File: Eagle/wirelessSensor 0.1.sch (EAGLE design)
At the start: 26 parts, among them U1 HDC1080, U2 PIC16F1823-X_SL, X1 22-23-2021

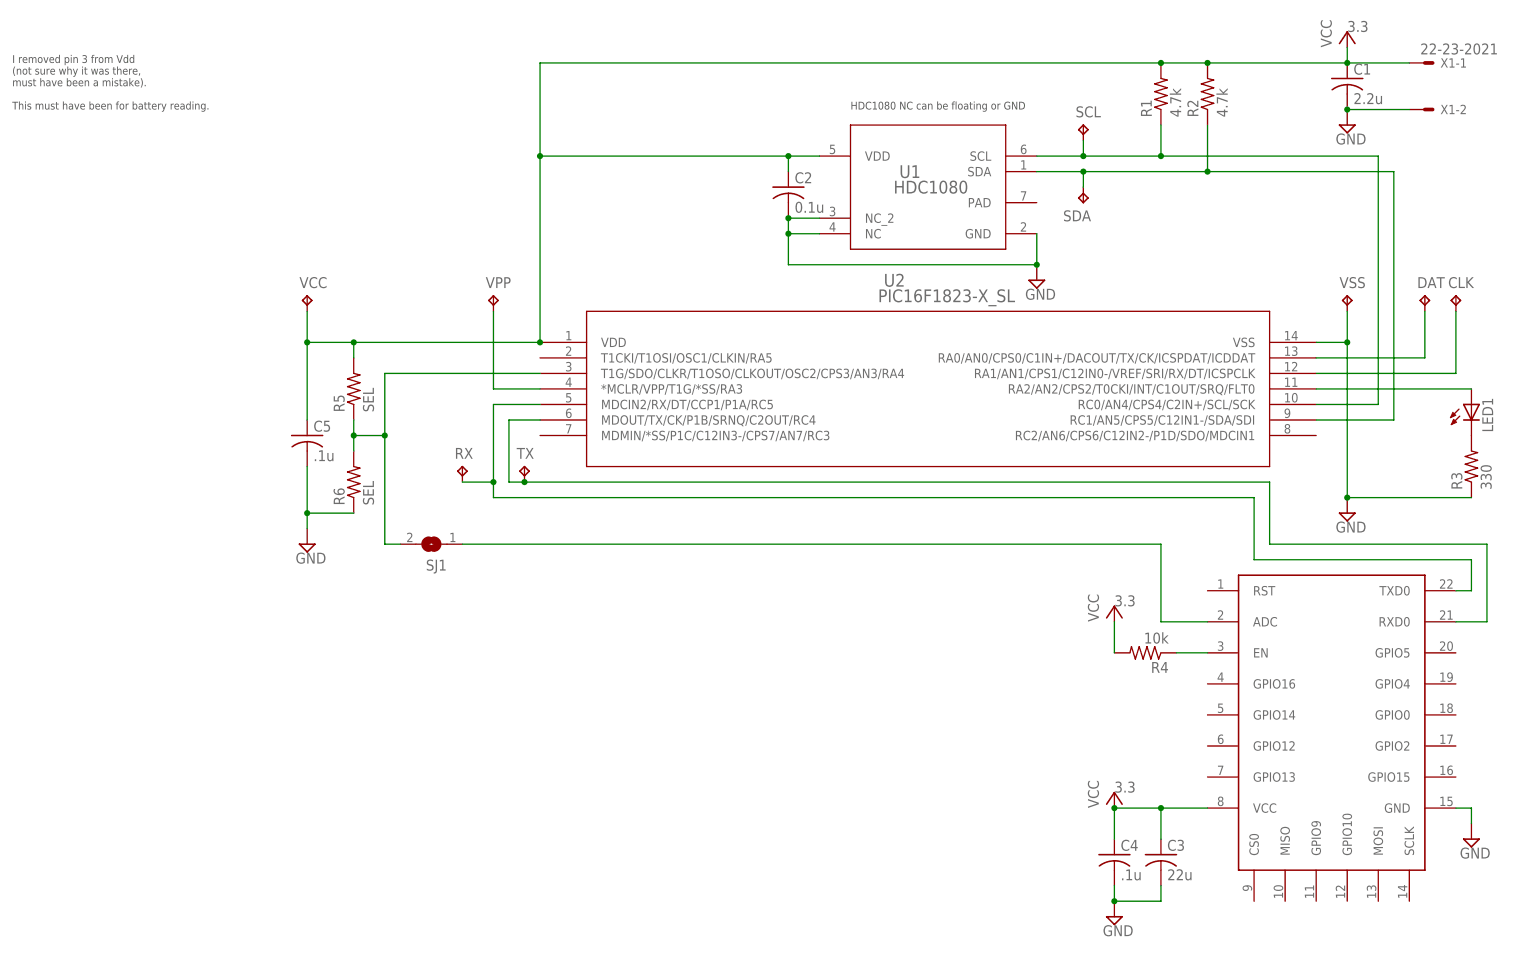
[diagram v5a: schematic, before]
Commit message: More work on the PCB, added some SeeedStudio specific files (cam generator, DRC rules)
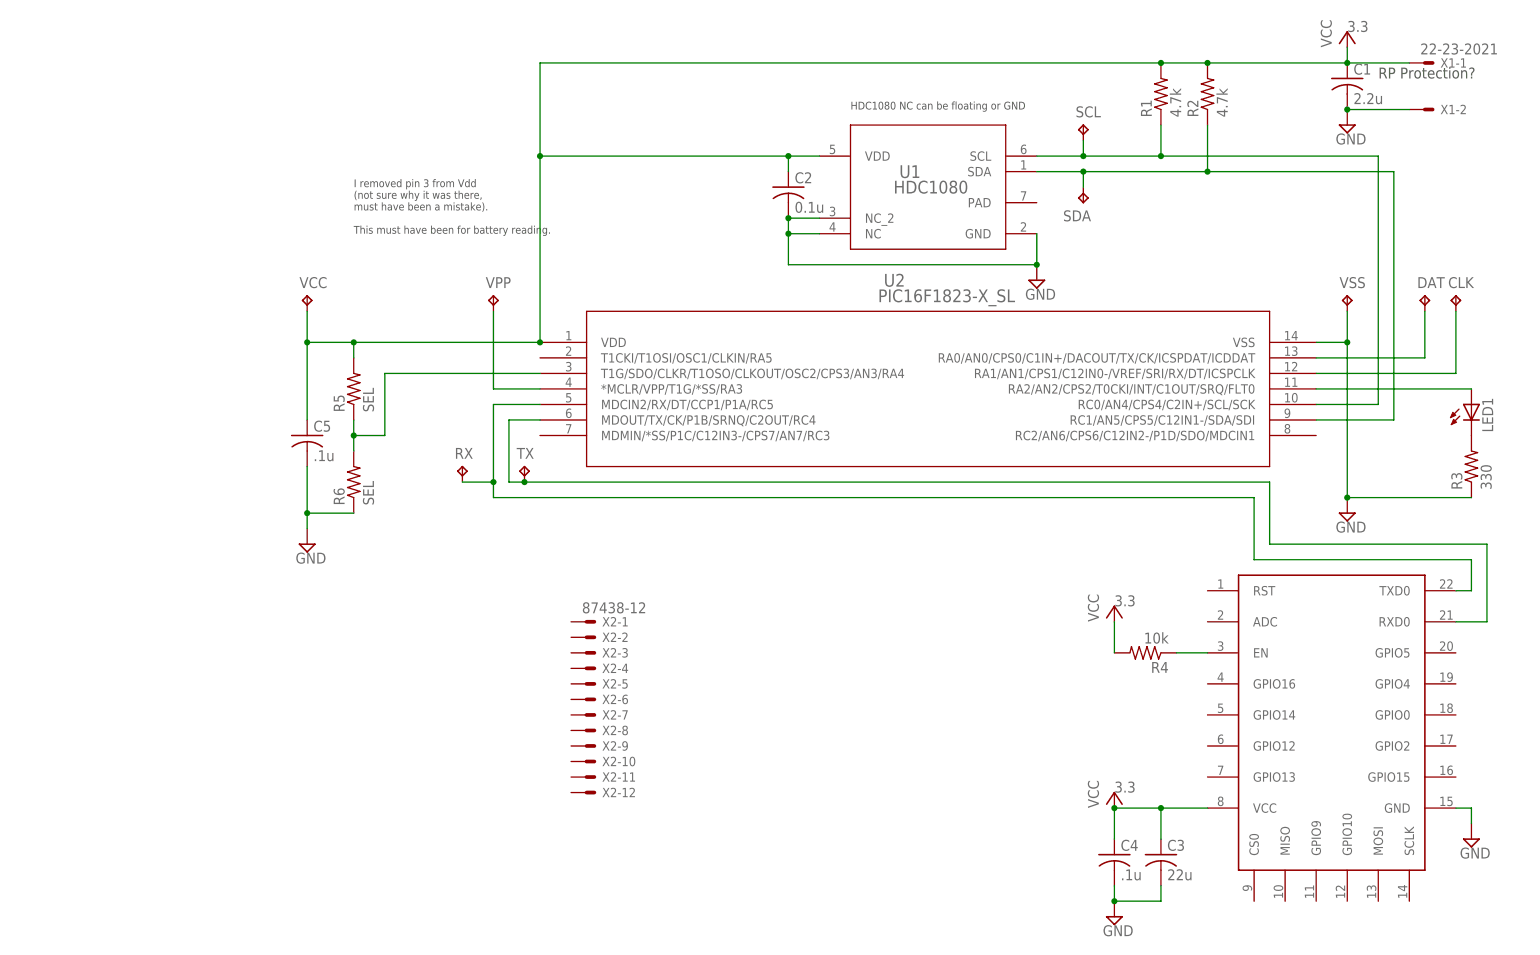
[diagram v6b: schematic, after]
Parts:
- removed SJ1: (no value), jumper:SJ
- added X2: 87438-12, con-molex:87438-12
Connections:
- removed net N$12: SJ1.1, U$1.ADC
- net N$9: no longer SJ1.2
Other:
- note added: "RP Protection?"
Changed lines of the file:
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@@
 <?xml version="1.0" encoding="utf-8"?>
 <!DOCTYPE eagle SYSTEM "eagle.dtd">
-<eagle version="7.7.0">
+<eagle version="7.6.0">
 <drawing>
 <settings>
@@
 <part name="R5" library="rcl" deviceset="R-US_" device="R0603" value="SEL"/>
 <part name="R6" library="rcl" deviceset="R-US_" device="R0603" value="SEL"/>
-<part name="SJ1" library="jumper" deviceset="SJ" device=""/>
+<part name="X2" library="con-molex" deviceset="87438-12" device=""/>
 </parts>
 <sheets>
 <sheet>
 <plain>
-<text x="-149.86" y="40.64" size="1.27" layer="97">I removed pin 3 from Vdd
+<text x="-93.98" y="20.32" size="1.27" layer="97">I removed pin 3 from Vdd
 (not sure why it was there,
 must have been a mistake).
 This must have been for battery reading.</text>
 <text x="-12.7" y="40.64" size="1.27" layer="97">HDC1080 NC can be floating or GND</text>
+<text x="73.66" y="45.72" size="1.778" layer="97">RP Protection?</text>
 </plain>
 <instances>
@@
 <instance part="R5" gate="G$1" x="-93.98" y="-5.08" rot="R90"/>
 <instance part="R6" gate="G$1" x="-93.98" y="-20.32" rot="R90"/>
-<instance part="SJ1" gate="1" x="-81.28" y="-30.48" rot="R180"/>
+<instance part="X2" gate="-1" x="-55.88" y="-43.18"/>
+<instance part="X2" gate="-2" x="-55.88" y="-45.72"/>
+<instance part="X2" gate="-3" x="-55.88" y="-48.26"/>
+<instance part="X2" gate="-4" x="-55.88" y="-50.8"/>
+<instance part="X2" gate="-5" x="-55.88" y="-53.34"/>
+<instance part="X2" gate="-6" x="-55.88" y="-55.88"/>
+<instance part="X2" gate="-7" x="-55.88" y="-58.42"/>
+<instance part="X2" gate="-8" x="-55.88" y="-60.96"/>
+<instance part="X2" gate="-9" x="-55.88" y="-63.5"/>
+<instance part="X2" gate="-10" x="-55.88" y="-66.04"/>
+<instance part="X2" gate="-11" x="-55.88" y="-68.58"/>
+<instance part="X2" gate="-12" x="-55.88" y="-71.12"/>
 </instances>
 <busses>
@@
 <pinref part="U2" gate="A" pin="T1G/SDO/CLKR/T1OSO/CLKOUT/OSC2/CPS3/AN3/RA4"/>
 <wire x1="-88.9" y1="-2.54" x2="-63.5" y2="-2.54" width="0.1524" layer="91"/>
-<pinref part="SJ1" gate="1" pin="2"/>
-<wire x1="-88.9" y1="-12.7" x2="-88.9" y2="-30.48" width="0.1524" layer="91"/>
-<wire x1="-88.9" y1="-30.48" x2="-86.36" y2="-30.48" width="0.1524" layer="91"/>
-<junction x="-88.9" y="-12.7"/>
-</segment>
-</net>
-<net name="N$12" class="0">
-<segment>
-<pinref part="SJ1" gate="1" pin="1"/>
-<wire x1="-76.2" y1="-30.48" x2="38.1" y2="-30.48" width="0.1524" layer="91"/>
-<wire x1="38.1" y1="-30.48" x2="38.1" y2="-43.18" width="0.1524" layer="91"/>
-<pinref part="U$1" gate="G$1" pin="ADC"/>
-<wire x1="38.1" y1="-43.18" x2="45.72" y2="-43.18" width="0.1524" layer="91"/>
-</segment>
-</net>
+</segment>
+</net>
